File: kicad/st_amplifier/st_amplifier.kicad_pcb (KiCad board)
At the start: 2 copper layers, 170 x 80 mm, 80 parts

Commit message: New commit.
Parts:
- added C37: 22 п, SMD0805, F.Cu at (213.4, 85.1)
- added C38: 22 п, SMD0805, F.Cu at (80.6, 85.1)
- R14, R2: value 28.7 к +/-0.5% -> 28 к +/-0.5%
- R6, R8: value 22.1 к +/-0.5% -> 24 к +/-0.5%
- moved C3 37.8 mm to (123.8, 126.4)
- moved C4 37.1 mm to (165.1, 112.4), turned to 270 degrees
- moved C2 36.2 mm to (122.6, 121.3), turned to 180 degrees
- moved XP1 29.2 mm to (82.5, 126.4)
- moved XP2 26.7 mm to (200.0, 126.4)
- moved DA2 19.4 mm to (151.8, 122.7), turned to 90 degrees
- moved C36 19.3 mm to (193.0, 87.6), turned to 270 degrees
- moved C30 18.9 mm to (184.2, 85.7)
- moved R16 18.8 mm to (190.5, 111.8)
- moved R6 18.8 mm to (189.2, 108.6)
- moved C12 18.8 mm to (191.8, 108.6)
- moved R19 18.5 mm to (196.2, 87.6)
- moved C5 18.5 mm to (163.8, 121.3), turned to 180 degrees
- moved 1_PIN 18.1 mm to (153.3, 116.7), turned to 90 degrees
- moved R26 17.8 mm to (155.6, 128.3)
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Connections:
- XP1 pad 1: /MU/ST -> /+29V
- XP1 pad 2: /+29V -> /MU/ST
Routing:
- net /GND: track 403.2 -> 364.0 mm
- net /CLIP_2: track 199.1 -> 164.3 mm, vias 2 -> 6
- net /+29V: track 313.5 -> 280.7 mm, vias 2 -> 1
- net /MU/ST: track 44.6 -> 13.1 mm
- net /+15V: track 21.7 -> 52.3 mm
- net N-0000022: track 50.8 -> 27.2 mm
- net N-000005: track 43.7 -> 28.0 mm, vias 2 -> 0
- net N-0000021: track 60.8 -> 48.8 mm
- net /MUTE: track 215.5 -> 204.4 mm, vias 4 -> 5
- net N-0000011: track 15.8 -> 26.8 mm, vias 0 -> 2
- net N-000002: track 106.2 -> 96.0 mm
- net /STBY: track 186.2 -> 176.0 mm, vias 5 -> 3
- net /-15V: track 22.6 -> 16.0 mm
- net /-29V: track 342.9 -> 336.4 mm
- net N-000003: track 8.91 -> 15.3 mm
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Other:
- board size 170 x 80 mm -> 164.5 x 70 mm
- board text added: "CL 1"
- board text added: "CL 2"
- board text removed: "CLIP 1"
- board text removed: "CLIP 2"

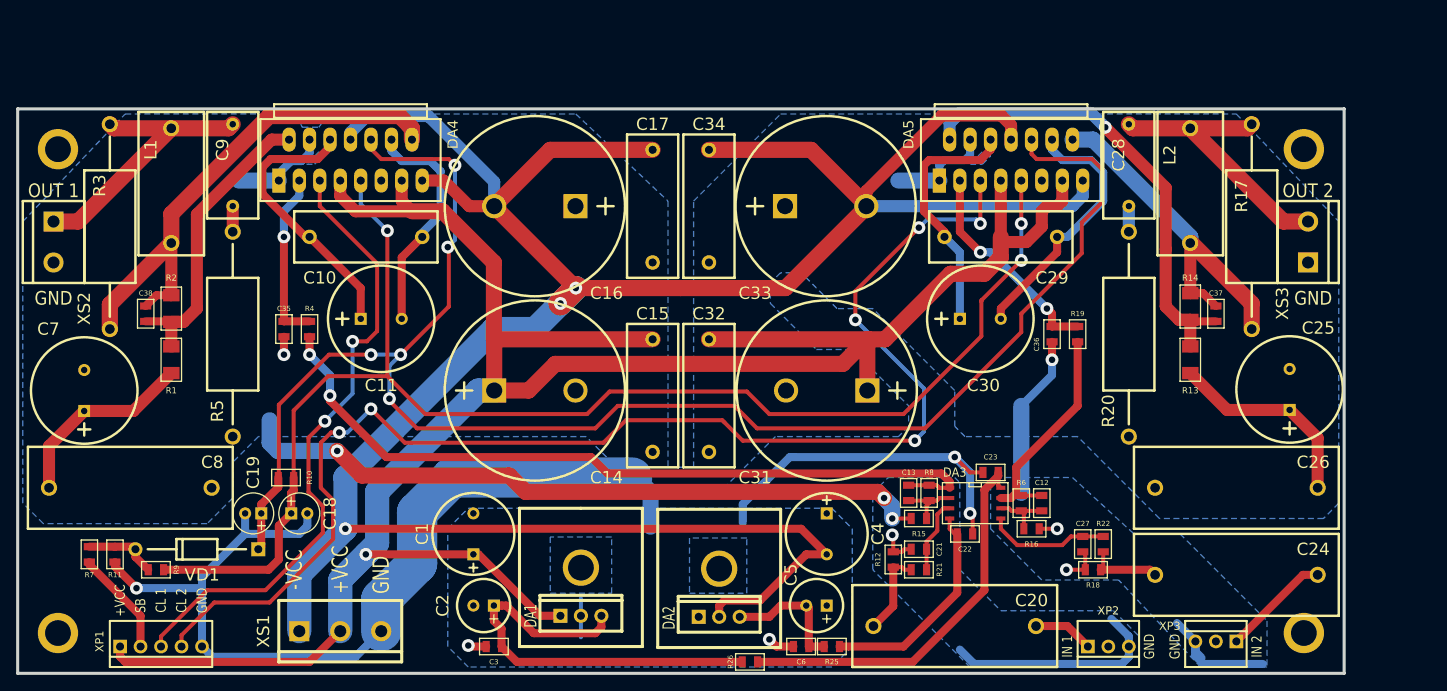
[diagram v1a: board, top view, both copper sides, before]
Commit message: Moved to kicad 4.0.0
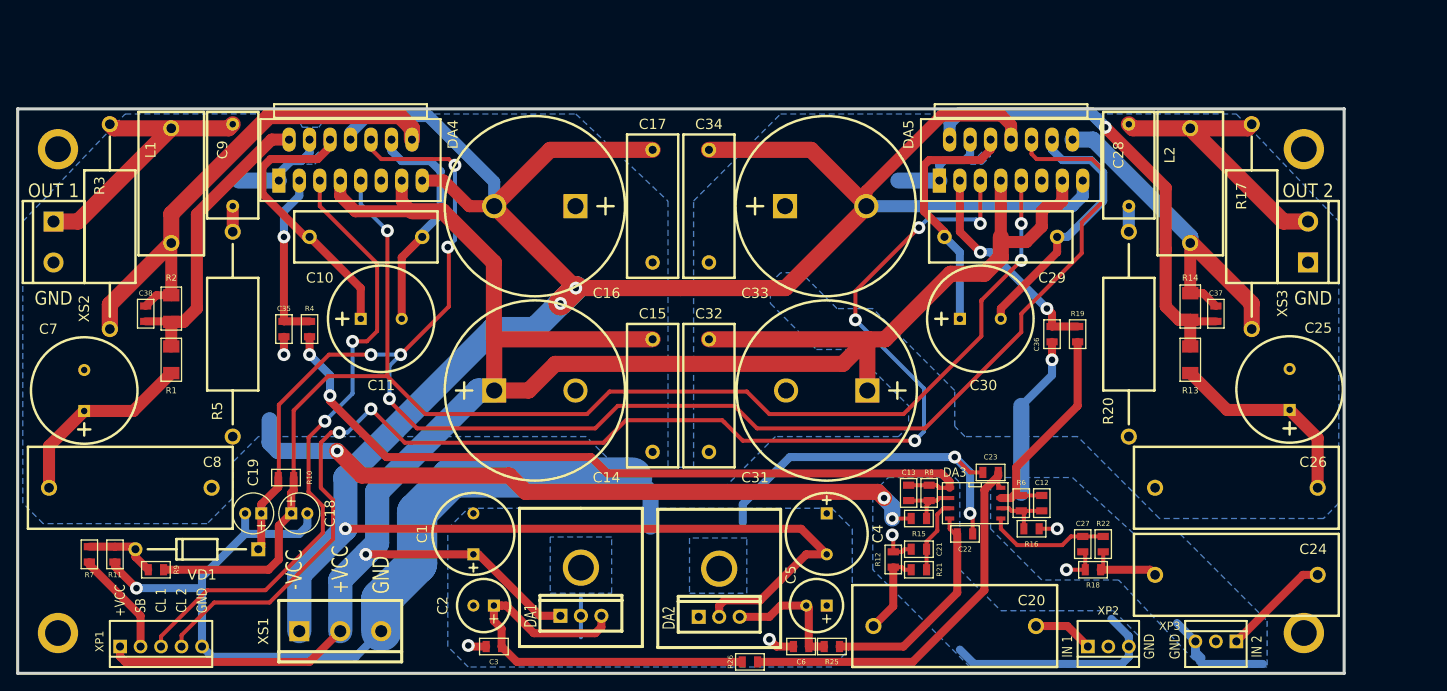
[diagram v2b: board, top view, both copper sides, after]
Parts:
- C28, C9: value 0.047 мк -> 0.1 мк
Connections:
- XP2 pad 2: (no net) -> Net-(XP2-Pad2)
- XP3 pad 2: (no net) -> Net-(XP3-Pad2)
